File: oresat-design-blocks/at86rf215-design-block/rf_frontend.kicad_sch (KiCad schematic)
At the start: 10 parts, among them J1 Conn_Coaxial, U2 2450FB15A050E

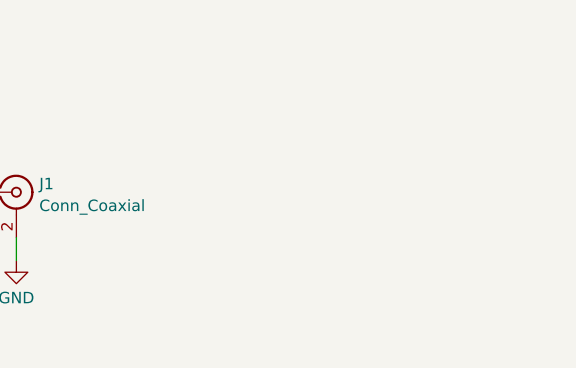
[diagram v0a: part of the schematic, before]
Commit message: added initial footprints and oreganized schematic. Started PCB
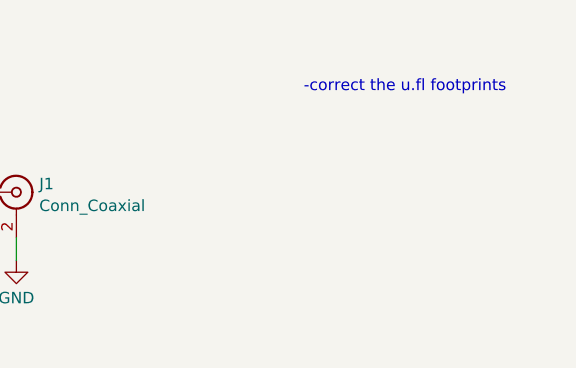
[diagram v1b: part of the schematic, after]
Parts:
- C1, C10, C11, C2, C4: footprint (none) -> Capacitor_SMD:C_0603_1608Metric
- J1: footprint (none) -> oresat-connectors:J-U.FL
- L1: footprint (none) -> Inductor_SMD:L_0603_1608Metric
- R2, R3: footprint (none) -> Resistor_SMD:R_0603_1608Metric
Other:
- note added: "-correct the u.fl footprints"
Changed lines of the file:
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@@
 	(generator_version "9.0")
 	(paper "A4")
+	(text "-correct the u.fl footprints"
+		(exclude_from_sim no)
+		(at 170.18 28.956 0)
+		(effects
+			(font
+				(size 1.27 1.27)
+			)
+		)
+	)
 	(text "sanity check on the footprint for this plz\nimported the footprint model for this but it seems \nslightly off in the distance between pads in the x direction"
 		(exclude_from_sim no)
@@
 			)
 		)
-		(property "Footprint" ""
+		(property "Footprint" "Capacitor_SMD:C_0603_1608Metric"
 			(at 43.18 40.64 0)
 			(effects
@@
 			)
 		)
-		(property "Footprint" ""
+		(property "Footprint" "Resistor_SMD:R_0603_1608Metric"
 			(at 116.84 44.45 0)
 			(effects
@@
 			)
 		)
-		(property "Footprint" ""
+		(property "Footprint" "Resistor_SMD:R_0603_1608Metric"
 			(at 100.33 40.64 0)
 			(effects
@@
 			)
 		)
-		(property "Footprint" ""
+		(property "Footprint" "Capacitor_SMD:C_0603_1608Metric"
 			(at 43.18 45.72 0)
 			(effects
@@
 			)
 		)
-		(property "Footprint" ""
+		(property "Footprint" "Inductor_SMD:L_0603_1608Metric"
 			(at 48.26 43.18 0)
 			(effects
@@
 			)
 		)
-		(property "Footprint" ""
+		(property "Footprint" "Capacitor_SMD:C_0603_1608Metric"
 			(at 86.36 40.64 0)
 			(effects
@@
 			)
 		)
-		(property "Footprint" ""
+		(property "Footprint" "Capacitor_SMD:C_0603_1608Metric"
 			(at 106.68 46.99 0)
 			(effects
@@
 			)
 		)
-		(property "Footprint" ""
+		(property "Footprint" "Capacitor_SMD:C_0603_1608Metric"
 			(at 93.98 46.99 0)
 			(effects
@@
 			)
 		)
-		(property "Footprint" ""
+		(property "Footprint" "oresat-connectors:J-U.FL"
 			(at 127 40.64 0)
 			(effects

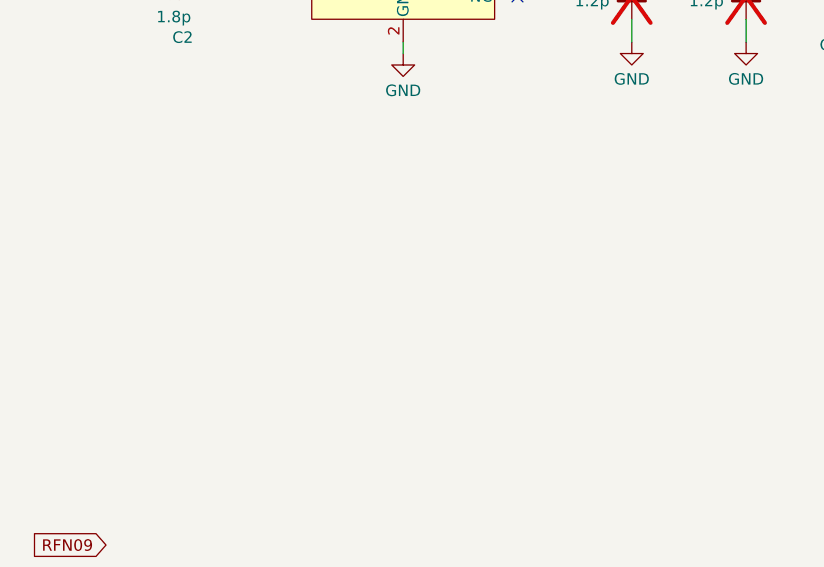
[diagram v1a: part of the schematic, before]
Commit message: First design review of AT86 eval board. Added 5V to 3.3V LDO with low noise, added USB C port, and found a Balun for UHF and L band.
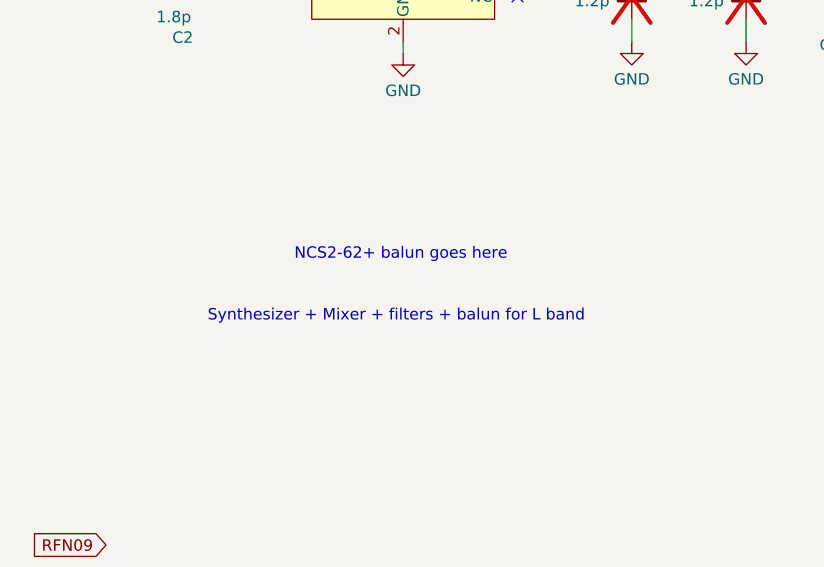
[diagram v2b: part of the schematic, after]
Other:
- note added: "NCS2-62+ balun goes here"
- note added: "Synthesizer + Mixer + filters + balun for L band"
- company: (none) -> Portland State Aerospace Society
- title: (none) -> OreSat AT86RF215 Evaluation Board
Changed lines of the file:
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@@
 	(generator "eeschema")
 	(generator_version "9.0")
-	(paper "A4")
+	(paper "B")
+	(title_block
+		(title "OreSat AT86RF215 Evaluation Board")
+		(date "2025-12-16")
+		(rev "1.0")
+		(company "Portland State Aerospace Society")
+	)
+	(text "Synthesizer + Mixer + filters + balun for L band"
+		(exclude_from_sim no)
+		(at 67.818 82.55 0)
+		(effects
+			(font
+				(size 1.27 1.27)
+			)
+		)
+	)
 	(text "-correct the u.fl footprints"
 		(exclude_from_sim no)
@@
 		(effects
 			(font
+				(size 1.27 1.27)
+			)
+		)
+	)
+	(text "NCS2-62+ balun goes here"
+		(exclude_from_sim no)
+		(at 68.326 75.692 0)
+		(effects
+			(font
